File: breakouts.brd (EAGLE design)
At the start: 160 x 100 mm, 7 parts

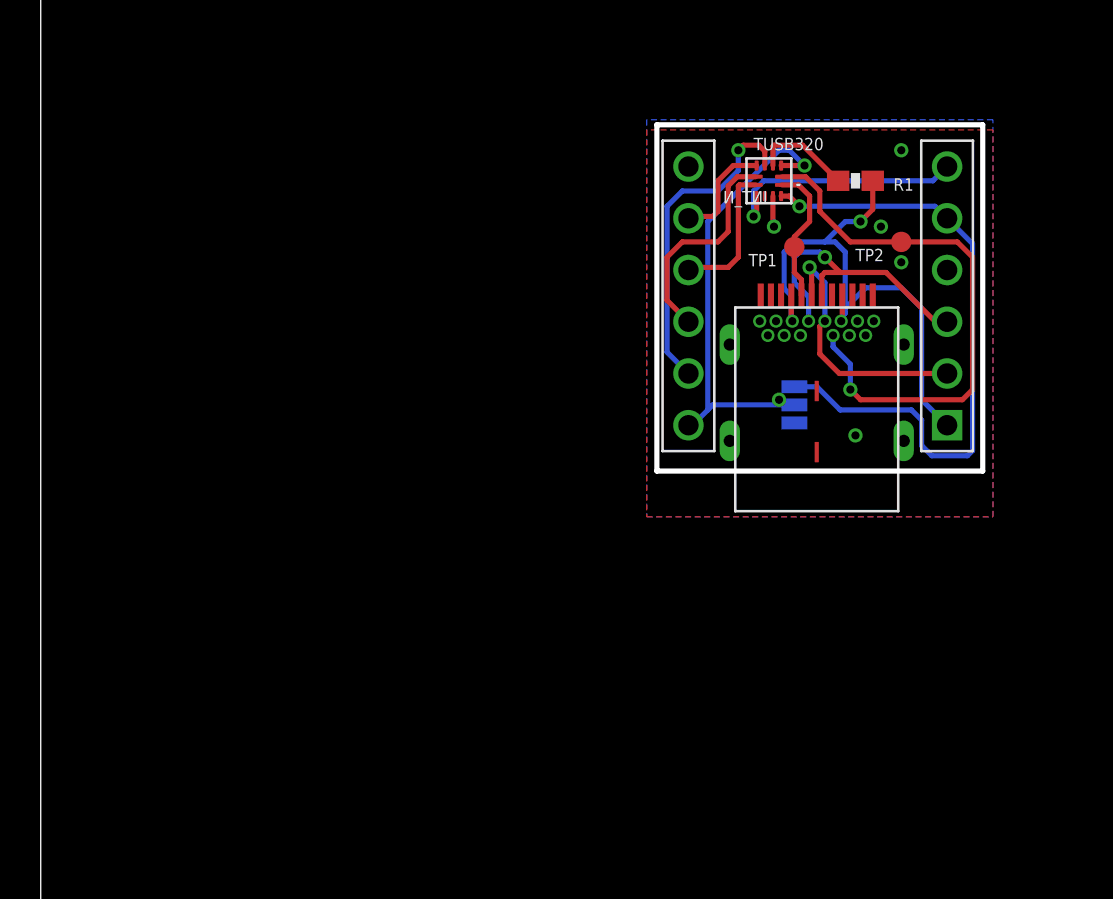
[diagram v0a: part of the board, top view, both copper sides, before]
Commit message: Added USB C breakout with CC pulldown resistors
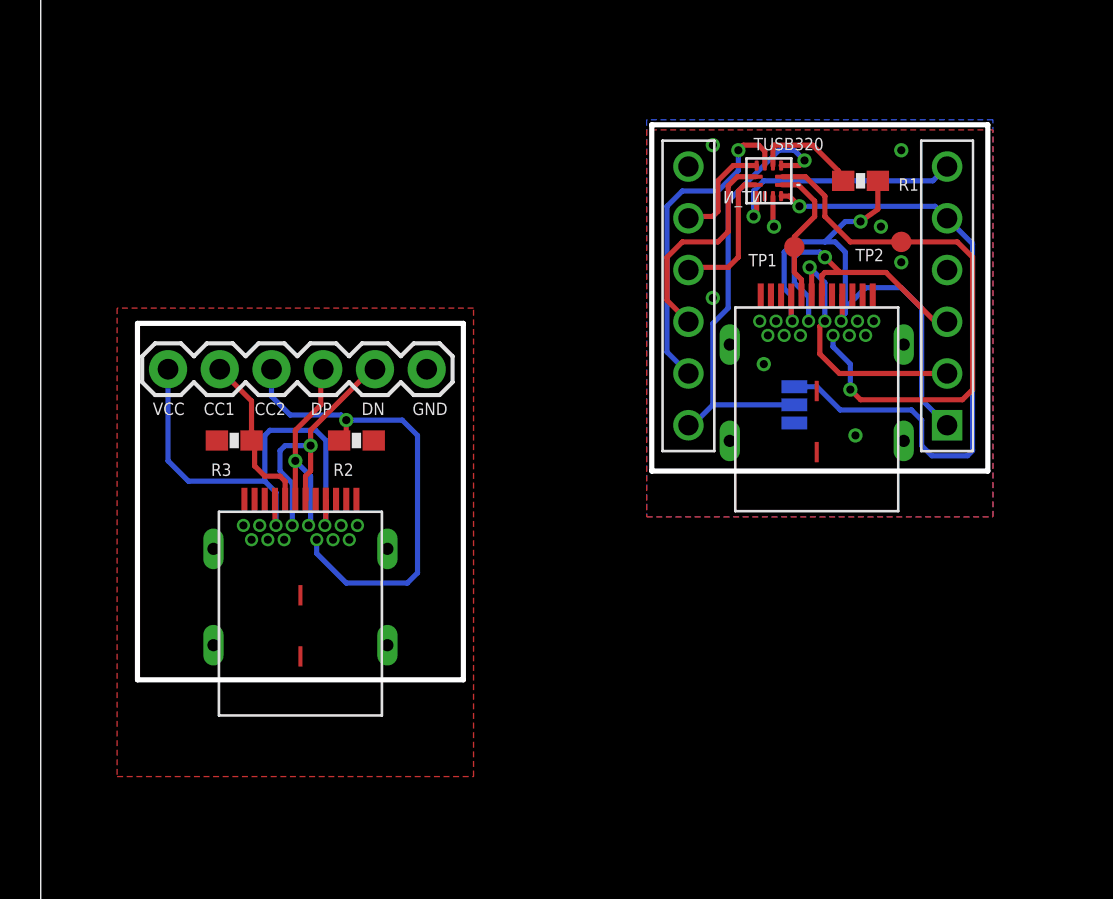
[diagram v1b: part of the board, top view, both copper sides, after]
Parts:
- added CONN2: USB-C_WURTH_632723X00011USB-C, USB-C:USB-C_WURTH_632723X00011
- added JP1: (no value), SparkFun:1X06
- added R2, R3: 5K1, SparkFun-Passives:0603-RES
- moved R1 0.25 mm to (40.2, 36.0)
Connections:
- removed net N$10: U$2.P$7
- new net CC1_SA: CONN2.A5, JP1.2, R3.2
- new net CC2_SA: CONN2.B5, JP1.3, R2.2
- new net DN_SA: CONN2.A7, CONN2.B7, JP1.5
- new net DP_SA: CONN2.A6, CONN2.B6, JP1.4
- new net VBUS_SA: CONN2.A4, CONN2.A9, CONN2.B4, CONN2.B9, JP1.1
- net GND: now also CONN1.GND1, CONN1.GND2, CONN1.GND3, CONN1.GND4, CONN2.A1, CONN2.A12, CONN2.B1, CONN2.B12, CONN2.CON1, CONN2.CON2, CONN2.CON3, CONN2.CON4, CONN2.GND1, CONN2.GND2, CONN2.GND3, CONN2.GND4, JP1.6, R2.1, R3.1
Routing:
- net VBUS_SA: track 0.00 -> 24.4 mm
- net CC2_SA: track 0.00 -> 23.6 mm, vias 0 -> 1
- net DN_SA: track 0.00 -> 13.4 mm, vias 0 -> 1
- net DP_SA: track 0.00 -> 10.5 mm, vias 0 -> 1
- net CC1_SA: track 0.00 -> 8.19 mm
- net GND: vias 6 -> 8
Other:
- outline, holes or cut-outs redrawn
- board text added: "CC1"
- board text added: "CC2"

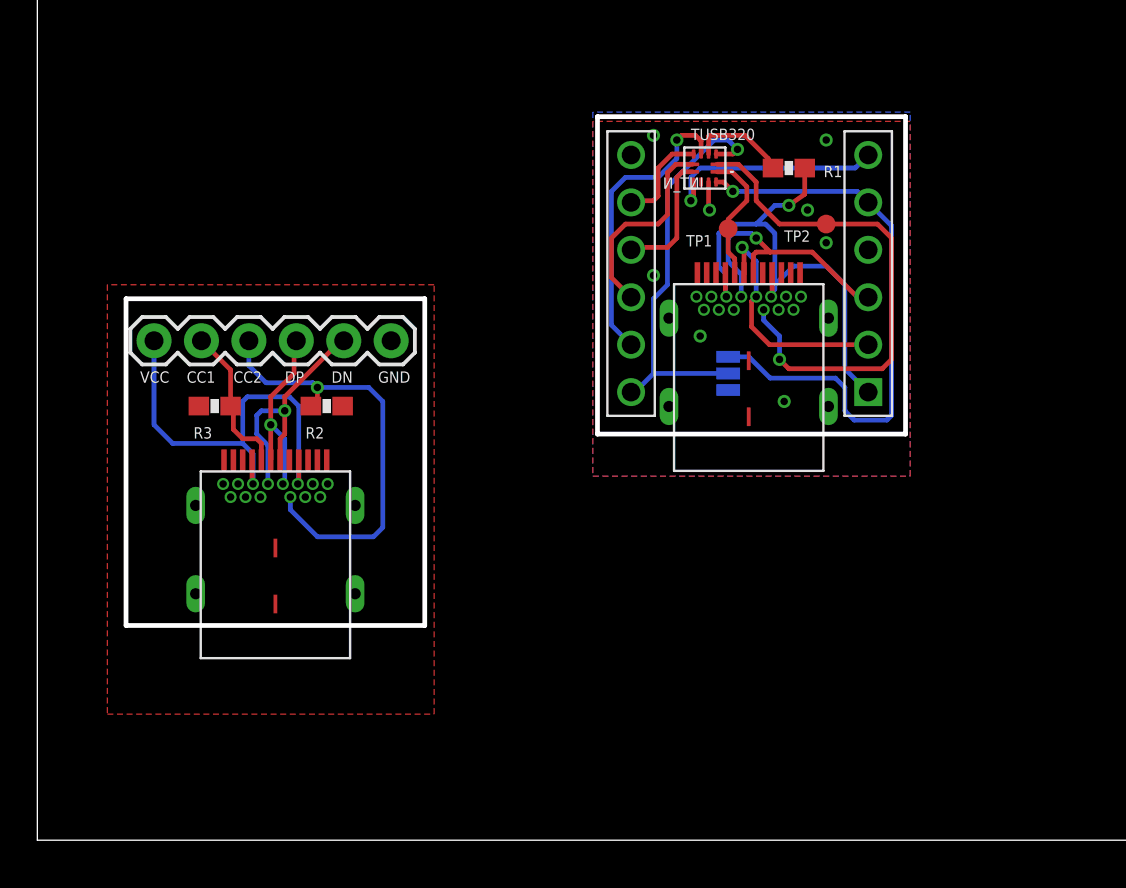
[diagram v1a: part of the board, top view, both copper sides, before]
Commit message: Added RJ12 breakout
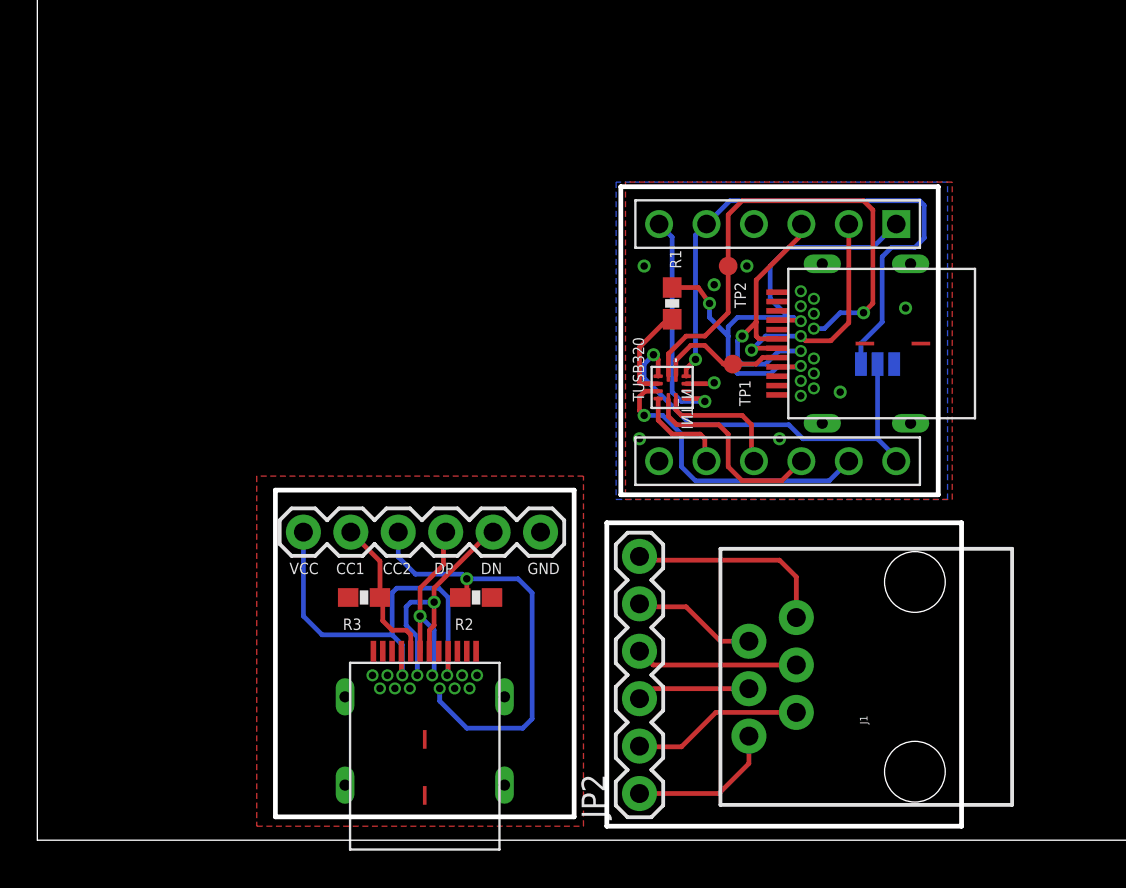
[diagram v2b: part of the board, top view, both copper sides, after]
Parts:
- added J1: RJ11, SparkFun-Connectors:RJ11-6
- added JP2: (no value), SparkFun:1X06
- moved CONN1 13.9 mm to (50.2, 26.6), turned to 90 degrees
- moved CONN2 13.0 mm to (20.8, -0.50)
- moved JP1 13.0 mm to (14.2, 16.5)
- moved R2 13.0 mm to (23.5, 13.0)
- moved R3 13.0 mm to (17.5, 13.0)
- moved U$1 11.9 mm to (34.0, 24.2), turned to 270 degrees
- moved R1 9.57 mm to (34.0, 28.8), turned to 270 degrees
- moved U$2 9.12 mm to (46.0, 33.0), turned to 270 degrees
- moved SJ1 8.02 mm to (45.0, 25.5), turned to 180 degrees
- moved TP1 7.25 mm to (37.2, 25.5), turned to 90 degrees
- moved TP2 5.71 mm to (37.0, 30.8), turned to 90 degrees
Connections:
- new net N$1: J1.1, JP2.1
- new net N$2: J1.2, JP2.2
- new net N$3: J1.3, JP2.3
- new net N$4: J1.4, JP2.4
- new net N$5: J1.5, JP2.5
- new net N$6: J1.6, JP2.6
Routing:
- net N$6: track 0.00 -> 11.0 mm
- net N$2: track 0.00 -> 9.18 mm
- net N$4: track 0.00 -> 8.70 mm
- net N$1: track 0.00 -> 7.99 mm
- net N$5: track 0.00 -> 6.69 mm
- net N$3: track 0.00 -> 6.08 mm
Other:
- outline, holes or cut-outs redrawn

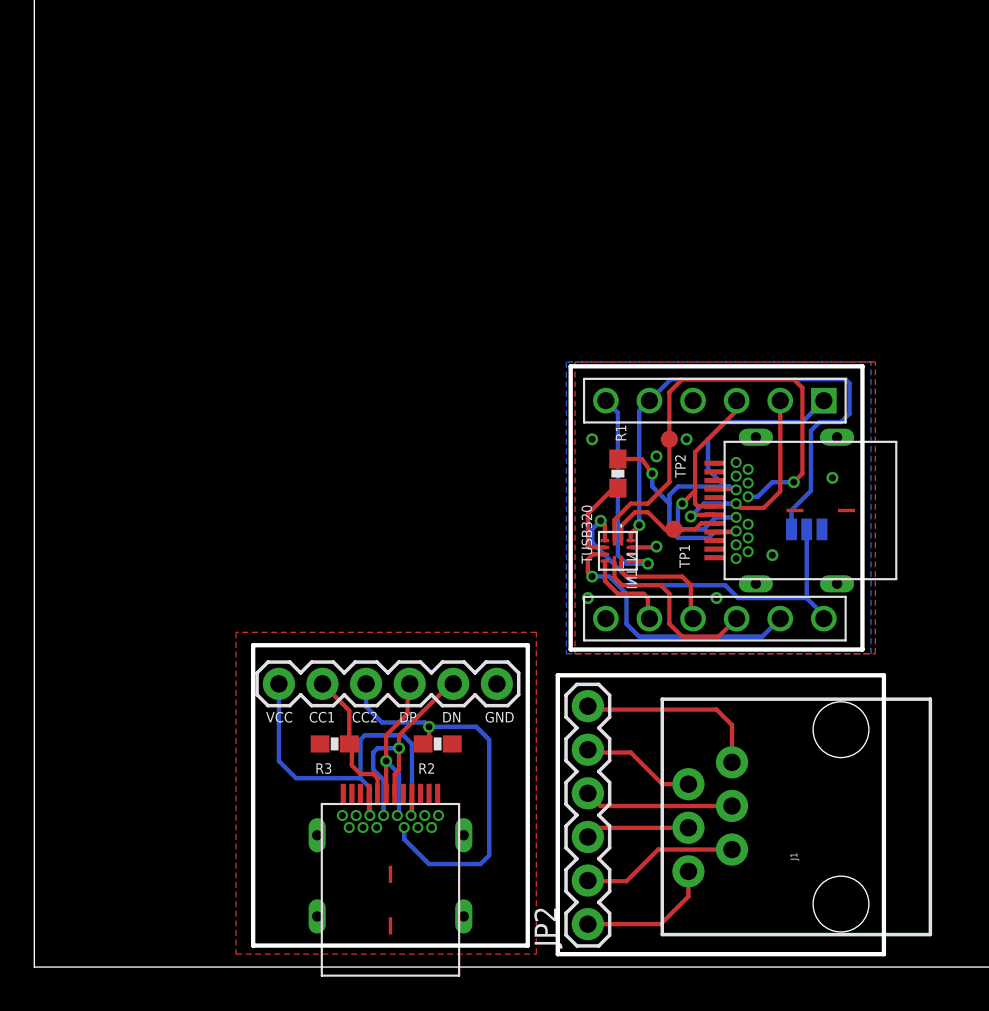
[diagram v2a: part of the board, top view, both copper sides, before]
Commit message: Panalised breakouts and added powerpole breakout
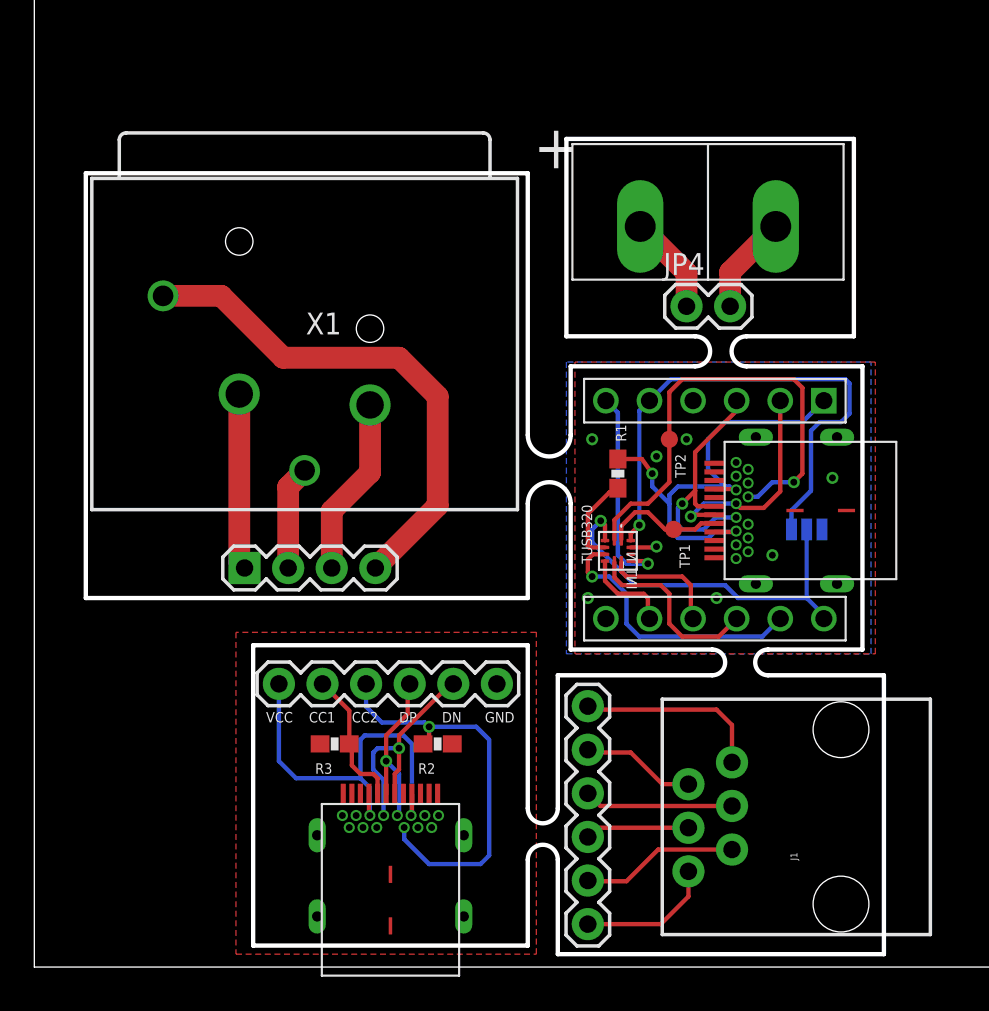
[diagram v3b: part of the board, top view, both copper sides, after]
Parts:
- added J2: POWERPOLE_POWER25A, powerpoles:POWERPOLE_PAIR_25A
- added JP3: (no value), SparkFun-Connectors:1X04
- added JP4: M02PTH, SparkFun-Connectors:1X02
- added X1: NC3FAH2-0, con-neutrik_ag:NC3FAH2-0
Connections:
- new net N$10: JP3.3, X1.2
- new net N$11: JP3.4, X1.G
- new net N$12: J2.RED, JP4.1
- new net N$13: J2.BLACK, JP4.2
- new net N$7: JP3.1, X1.1
- new net N$8: JP3.2, X1.3
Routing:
- net N$11: track 0.00 -> 29.9 mm
- net N$10: track 0.00 -> 10.4 mm
- net N$7: track 0.00 -> 10.3 mm
- net N$8: track 0.00 -> 6.08 mm
- net N$12: track 0.00 -> 5.77 mm
- net N$13: track 0.00 -> 5.75 mm
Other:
- outline, holes or cut-outs redrawn
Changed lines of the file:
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@@
 <wire x1="160" y1="100" x2="0" y2="100" width="0" layer="20"/>
 <wire x1="0" y1="100" x2="0" y2="0" width="0" layer="20"/>
-<wire x1="31.25" y1="18.5" x2="48.25" y2="18.5" width="0.254" layer="20"/>
-<wire x1="48.25" y1="18.5" x2="48.25" y2="35" width="0.254" layer="20"/>
-<wire x1="48.25" y1="35" x2="31.25" y2="35" width="0.254" layer="20"/>
-<wire x1="31.25" y1="35" x2="31.25" y2="18.5" width="0.254" layer="20"/>
 <dimension x1="0" y1="0" x2="50" y2="0" x3="25" y3="-9" textsize="1.778" layer="20"/>
 <dimension x1="0" y1="0" x2="0" y2="50" x3="-19" y3="25" textsize="1.778" layer="20"/>
@@
 <wire x1="12.75" y1="1.25" x2="12.75" y2="18.75" width="0.254" layer="20"/>
 <wire x1="12.75" y1="18.75" x2="28.75" y2="18.75" width="0.254" layer="20"/>
-<wire x1="28.75" y1="18.75" x2="28.75" y2="1.25" width="0.254" layer="20"/>
+<wire x1="28.75" y1="18.75" x2="28.75" y2="9.25" width="0.254" layer="20"/>
+<wire x1="28.75" y1="6.25" x2="28.75" y2="1.25" width="0.254" layer="20"/>
 <text x="13.5" y="14.25" size="0.6096" layer="25" font="vector">VCC</text>
 <text x="16" y="14.25" size="0.6096" layer="25" font="vector">CC1</text>
@@
 <text x="23.75" y="14.25" size="0.6096" layer="25" font="vector">DN</text>
 <text x="26.25" y="14.25" size="0.6096" layer="25" font="vector">GND</text>
-<wire x1="30.5" y1="17" x2="30.5" y2="0.75" width="0.254" layer="20"/>
+<wire x1="30.5" y1="17" x2="30.5" y2="9.25" width="0.254" layer="20"/>
+<wire x1="30.5" y1="9.25" x2="28.75" y2="9.25" width="0.254" layer="20" curve="-180"/>
+<wire x1="28.75" y1="6.25" x2="30.5" y2="6.25" width="0.254" layer="20" curve="-180"/>
+<wire x1="30.5" y1="6.25" x2="30.5" y2="0.75" width="0.254" layer="20"/>
 <wire x1="30.5" y1="0.75" x2="49.5" y2="0.75" width="0.254" layer="20"/>
 <wire x1="49.5" y1="0.75" x2="49.5" y2="17" width="0.254" layer="20"/>
-<wire x1="49.5" y1="17" x2="30.5" y2="17" width="0.254" layer="20"/>
+<wire x1="49.5" y1="17" x2="42.75" y2="17" width="0.254" layer="20"/>
+<wire x1="42.75" y1="17" x2="42.75" y2="18.5" width="0.254" layer="20" curve="-180"/>
+<wire x1="42.75" y1="18.5" x2="48.25" y2="18.5" width="0.254" layer="20"/>
+<wire x1="48.25" y1="18.5" x2="48.25" y2="35" width="0.254" layer="20"/>
+<wire x1="48.25" y1="35" x2="41.5" y2="35" width="0.254" layer="20"/>
+<wire x1="41.5" y1="35" x2="41.5" y2="36.75" width="0.254" layer="20" curve="-180"/>
+<wire x1="41.5" y1="36.75" x2="47.75" y2="36.75" width="0.254" layer="20"/>
+<wire x1="31" y1="36.75" x2="38.5" y2="36.75" width="0.254" layer="20"/>
+<wire x1="38.5" y1="36.75" x2="38.5" y2="35" width="0.254" layer="20" curve="-180"/>
+<wire x1="38.5" y1="35" x2="31.25" y2="35" width="0.254" layer="20"/>
+<wire x1="31.25" y1="35" x2="31.25" y2="31" width="0.254" layer="20"/>
+<wire x1="31.25" y1="31" x2="28.75" y2="31" width="0.254" layer="20" curve="-180"/>
+<wire x1="28.75" y1="31" x2="28.75" y2="46.25" width="0.254" layer="20"/>
+<wire x1="28.75" y1="21.5" x2="28.75" y2="27" width="0.254" layer="20"/>
+<wire x1="28.75" y1="27" x2="31.25" y2="27" width="0.254" layer="20" curve="-180"/>
+<wire x1="31.25" y1="27" x2="31.25" y2="18.5" width="0.254" layer="20"/>
+<wire x1="31.25" y1="18.5" x2="39.5" y2="18.5" width="0.254" layer="20"/>
+<wire x1="39.5" y1="18.5" x2="39.5" y2="17" width="0.254" layer="20" curve="-180"/>
+<wire x1="39.5" y1="17" x2="30.5" y2="17" width="0.254" layer="20"/>
+<wire x1="3" y1="46.25" x2="3" y2="21.5" width="0.254" layer="20"/>
+<wire x1="3" y1="21.5" x2="28.75" y2="21.5" width="0.254" layer="20"/>
+<wire x1="28.75" y1="46.25" x2="3" y2="46.25" width="0.254" layer="20"/>
+<wire x1="31" y1="48.25" x2="31" y2="36.75" width="0.254" layer="20"/>
+<wire x1="47.75" y1="36.75" x2="47.75" y2="48.25" width="0.254" layer="20"/>
+<wire x1="47.75" y1="48.25" x2="31" y2="48.25" width="0.254" layer="20"/>
 </plain>
 <attributes>
@@
 <attribute name="PROD_ID" value="CONN-08590" x="47" y="8.75" size="0.6096" layer="27" font="vector" rot="R90" display="off"/>
 </element>
-<element name="JP2" library="SparkFun" package="1X06" value="" x="32.25" y="2.5" rot="R90"/>
+<element name="JP2" library="SparkFun" package="1X06" value="" x="32.25" y="2.5" smashed="yes" rot="R90">
+<attribute name="VALUE" x="35.425" y="1.23" size="1.27" layer="27" rot="R90"/>
+</element>
+<element name="X1" library="con-neutrik_ag" package="NC3FAH2-0" value="NC3FAH2-0" x="15.75" y="32.75" smashed="yes">
+<attribute name="OC_NEWARK" value="11J5829" x="15.75" y="32.75" size="0.6096" layer="27" font="vector" display="off"/>
+<attribute name="MPN" value="NC3FAH-2-0" x="15.75" y="32.75" size="0.6096" layer="27" font="vector" display="off"/>
+<attribute name="MF" value="" x="15.75" y="32.75" size="0.6096" layer="27" font="vector" display="off"/>
+<attribute name="OC_FARNELL" value="unknown" x="15.75" y="32.75" size="0.6096" layer="27" font="vector" display="off"/>
+<attribute name="NAME" x="15.82" y="36.86" size="1.27" layer="25"/>
+<attribute name="VALUE" x="15.73" y="38.86" size="1.27" layer="27"/>
+</element>
+<element name="JP3" library="SparkFun-Connectors" package="1X04" value="" x="12.25" y="23.25" smashed="yes">
+<attribute name="VALUE" x="10.98" y="20.075" size="1.27" layer="27"/>
+</element>
+<element name="J2" library="powerpoles" package="POWERPOLE_PAIR_25A" value="POWERPOLE_POWER25A" x="39.25" y="44"/>
+<element name="JP4" library="SparkFun-Connectors" package="1X02" value="M02PTH" x="38" y="38.5"/>
 </elements>
 <signals>
@@
 <wire x1="32.45" y1="15" x2="32.25" y2="15.2" width="0.254" layer="1"/>
 </signal>
+<signal name="N$7">
+<contactref element="JP3" pad="1"/>
+<contactref element="X1" pad="1"/>
+<wire x1="11.94" y1="33.385" x2="11.94" y2="23.56" width="1.27" layer="1"/>
+<wire x1="11.94" y1="23.56" x2="12.25" y2="23.25" width="1.27" layer="1"/>
+</signal>
+<signal name="N$8">
+<contactref element="X1" pad="3"/>
+<contactref element="JP3" pad="2"/>
+<wire x1="14.79" y1="23.25" x2="14.79" y2="27.975" width="1.27" layer="1"/>
+<wire x1="14.79" y1="27.975" x2="15.75" y2="28.935" width="1.27" layer="1"/>
+</signal>
+<signal name="N$10">
+<contactref element="JP3" pad="3"/>
+<contactref element="X1" pad="2"/>
+<wire x1="19.56" y1="32.75" x2="19.56" y2="28.81" width="1.27" layer="1"/>
+<wire x1="19.56" y1="28.81" x2="17.33" y2="26.58" width="1.27" layer="1"/>
+<wire x1="17.33" y1="26.58" x2="17.33" y2="23.25" width="1.27" layer="1"/>
+</signal>
+<signal name="N$11">
+<contactref element="X1" pad="G"/>
+<contactref element="JP3" pad="4"/>
+<wire x1="19.87" y1="23.25" x2="23.5" y2="26.88" width="1.27" layer="1"/>
+<wire x1="23.5" y1="26.88" x2="23.5" y2="33.25" width="1.27" layer="1"/>
+<wire x1="23.5" y1="33.25" x2="21.25" y2="35.5" width="1.27" layer="1"/>
+<wire x1="21.25" y1="35.5" x2="14.5" y2="35.5" width="1.27" layer="1"/>
+<wire x1="14.5" y1="35.5" x2="10.895" y2="39.105" width="1.27" layer="1"/>
+<wire x1="10.895" y1="39.105" x2="7.5" y2="39.105" width="1.27" layer="1"/>
+</signal>
+<signal name="N$12">
+<contactref element="J2" pad="RED"/>
+<contactref element="JP4" pad="1"/>
+<wire x1="35.3" y1="43.15" x2="38" y2="40.45" width="1.27" layer="1"/>
+<wire x1="38" y1="40.45" x2="38" y2="38.5" width="1.27" layer="1"/>
+</signal>
+<signal name="N$13">
+<contactref element="J2" pad="BLACK"/>
+<contactref element="JP4" pad="2"/>
+<wire x1="43.2" y1="43.15" x2="40.54" y2="40.49" width="1.27" layer="1"/>
+<wire x1="40.54" y1="40.49" x2="40.54" y2="38.5" width="1.27" layer="1"/>
+</signal>
 </signals>
